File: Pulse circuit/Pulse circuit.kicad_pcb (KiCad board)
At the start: 4 copper layers, 76.9 x 88 mm, 9 parts, among them J1 Conn_01x02_Pin, U1 module_max30102, U2 module_max30102, U3 DOIT-ESP32-DEVKIT-V1

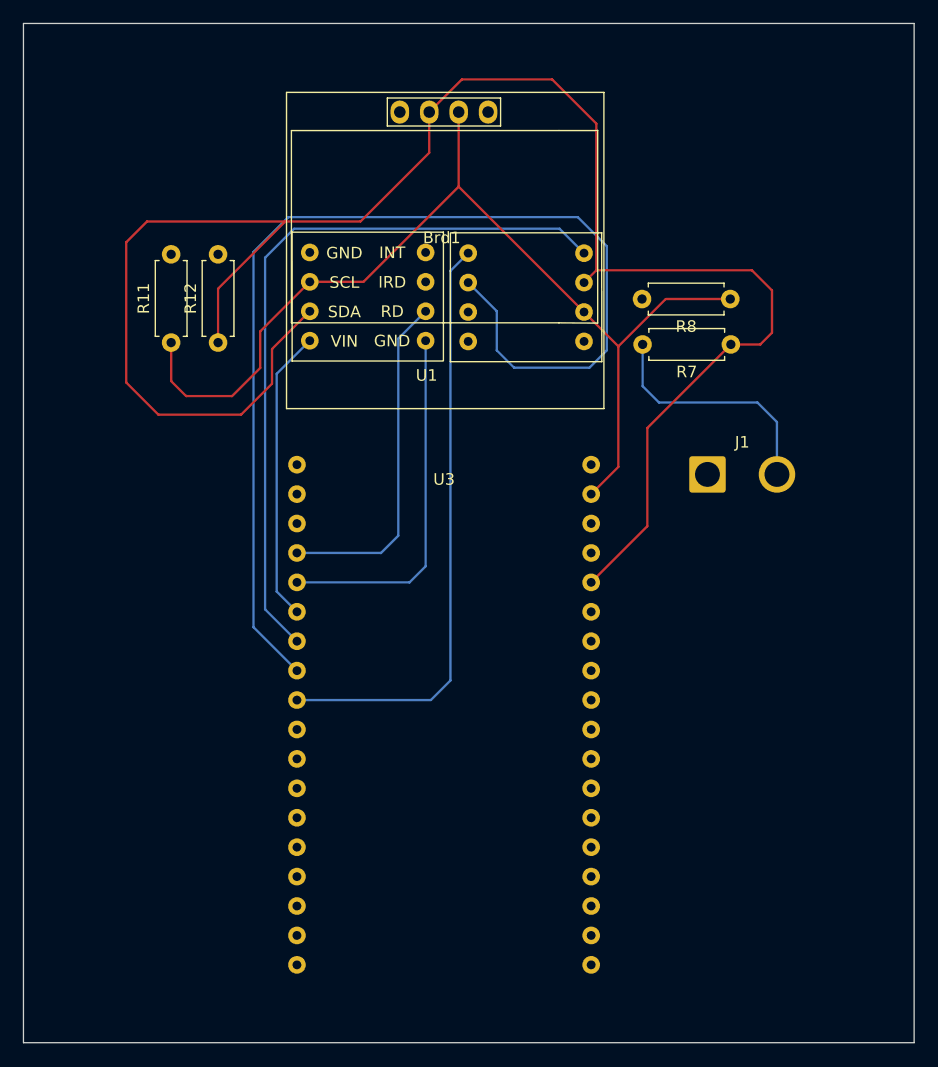
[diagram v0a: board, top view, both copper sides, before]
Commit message: Final design
Need to double check size of esp32
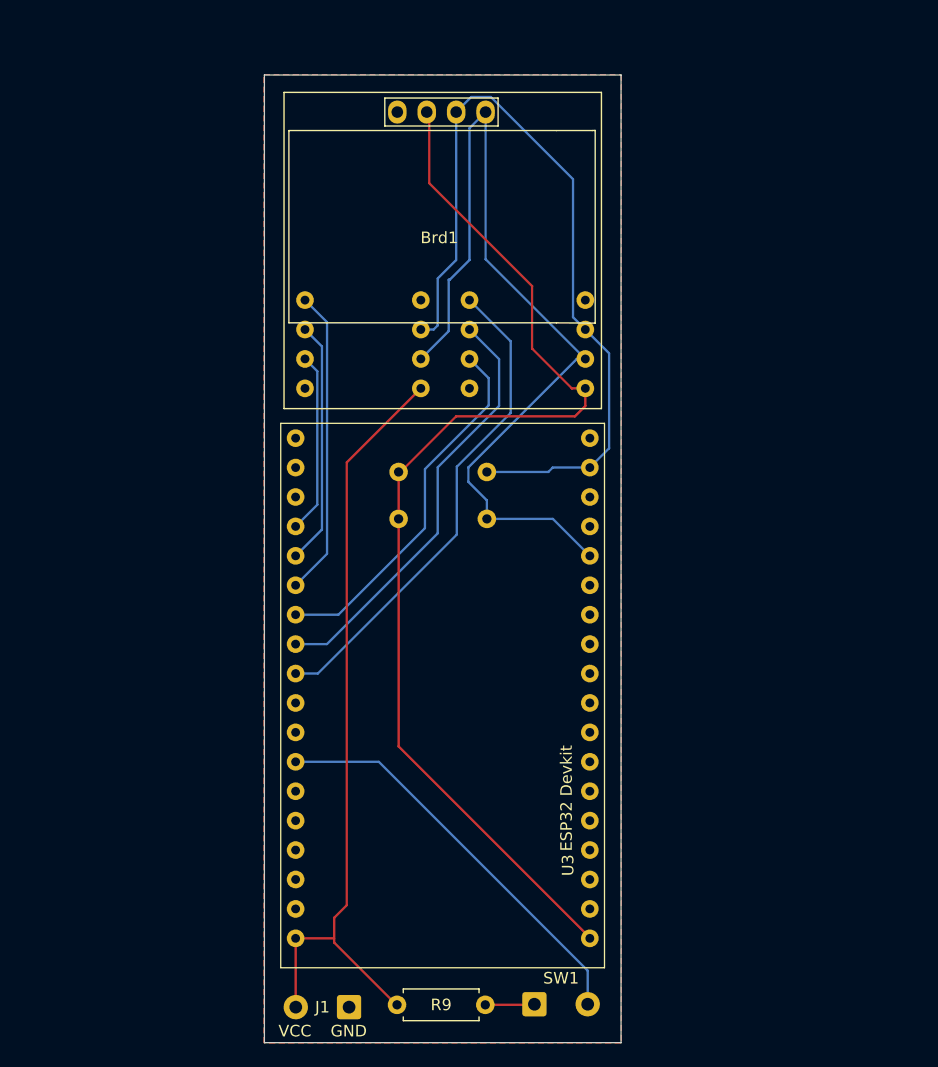
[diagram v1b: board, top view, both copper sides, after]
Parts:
- removed R7, R8: 10k, Resistor_THT:R_Axial_DIN0207_L6.3mm_D2.5mm_P7.62mm_Horizontal
- added R9: 1K, Resistor_THT:R_Axial_DIN0207_L6.3mm_D2.5mm_P7.62mm_Horizontal, F.Cu at (155.5, 126.5)
- added SW1: SW_Push, Connector_Wire:SolderWire-0.5sqmm_1x02_P4.6mm_D0.9mm_OD2.1mm, F.Cu at (159.8, 126.5)
- J1: footprint Connector_Wire:SolderWire-1.5sqmm_1x02_P6mm_D1.7mm_OD3mm -> Connector_Wire:SolderWire-0.5sqmm_1x02_P4.6mm_D0.9mm_OD2.1mm
- R11, R12, U1, U2: moved to B.Cu
- moved J1 55.4 mm to (143.8, 126.7), turned to 180 degrees
- moved U2 30.3 mm to (136.3, 60.2), turned to 0 degrees
- moved R11 29.5 mm to (155.6, 80.5), turned to 180 degrees
- moved R12 27.8 mm to (155.6, 84.5), turned to 180 degrees
- moved U1 20.0 mm to (150.5, 60.2)
- moved U3 2.29 mm to (151.8, 75.0)
- moved Brd1 0.22 mm to (151.5, 60.0)
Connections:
- Brd1 pad 2: SDA -> 3V3
- Brd1 pad 4: 3V3 -> SDA
- U1 pad 1: 3V3 -> GND
- U1 pad 2: SCL -> RD3v3
- U1 pad 3: SDA -> IRD3v3
- U1 pad 5: IRD3v3 -> GND
- U1 pad 6: RD3v3 -> SCL
- U1 pad 7: GND -> SDA
- U1 pad 8: (no net) -> 3V3
- U2 pad 1: 5V -> GND
- U2 pad 2: SCL -> RD5v
- U2 pad 3: SDA -> IRD5v
- U2 pad 5: IRD5v -> GND
- U2 pad 6: RD5v -> SCL
- U2 pad 7: GND -> SDA
- U2 pad 8: (no net) -> 5V
- U3 pad 4: RD3v3 -> RD5v
- U3 pad 5: IRD3v3 -> IRD5v
- U3 pad 6: INT3v3 -> INT5v
- U3 pad 7: INT5v -> RD3v3
- U3 pad 8: RD5v -> IRD3v3
- U3 pad 9: IRD5v -> INT3v3
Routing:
- net 3V3: track 0.00 -> 97.1 mm
- net SDA: track 160.7 -> 77.9 mm
- net RD5v: track 97.1 -> 15.7 mm
- net 5V: track 21.6 -> 67.8 mm
- net INT5v: track 63.7 -> 26.5 mm
- net B: track 0.00 -> 35.6 mm
- net IRD5v: track 51.5 -> 21.1 mm
- net SCL: track 89.0 -> 70.2 mm
- net INT3v3: track 25.3 -> 42.5 mm
- net IRD3v3: track 31.2 -> 37.1 mm
- net Net-(R9-Pad1): track 0.00 -> 4.26 mm
- net RD3v3: track 29.7 -> 31.8 mm
- added copper zone on F.Cu, net GND
- removed copper zone on In1.Cu, net 3V3
- removed copper zone on In1.Cu, net 5V
- removed copper zone on In2.Cu, net GND
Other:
- board size 76.9 x 88 mm -> 30.8 x 83.5 mm
- copper layers 4 -> 2
- board text added: "ESP32 Devkit"
- board text added: "GND"
- board text added: "VCC"
